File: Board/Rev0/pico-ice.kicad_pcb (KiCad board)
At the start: 2 copper layers, 52 x 51 mm, 34 parts, among them J1 USB_B_Micro, J2 Conn_01x02, J3 Conn_02x18_Odd_Even, J4 Conn_02x18_Odd_Even, U1 NCP1117-3.3_SOT223, U2 W25Q128JVS, U3 RP2040, Y1 ABLS-12.000MHZ-B4-T

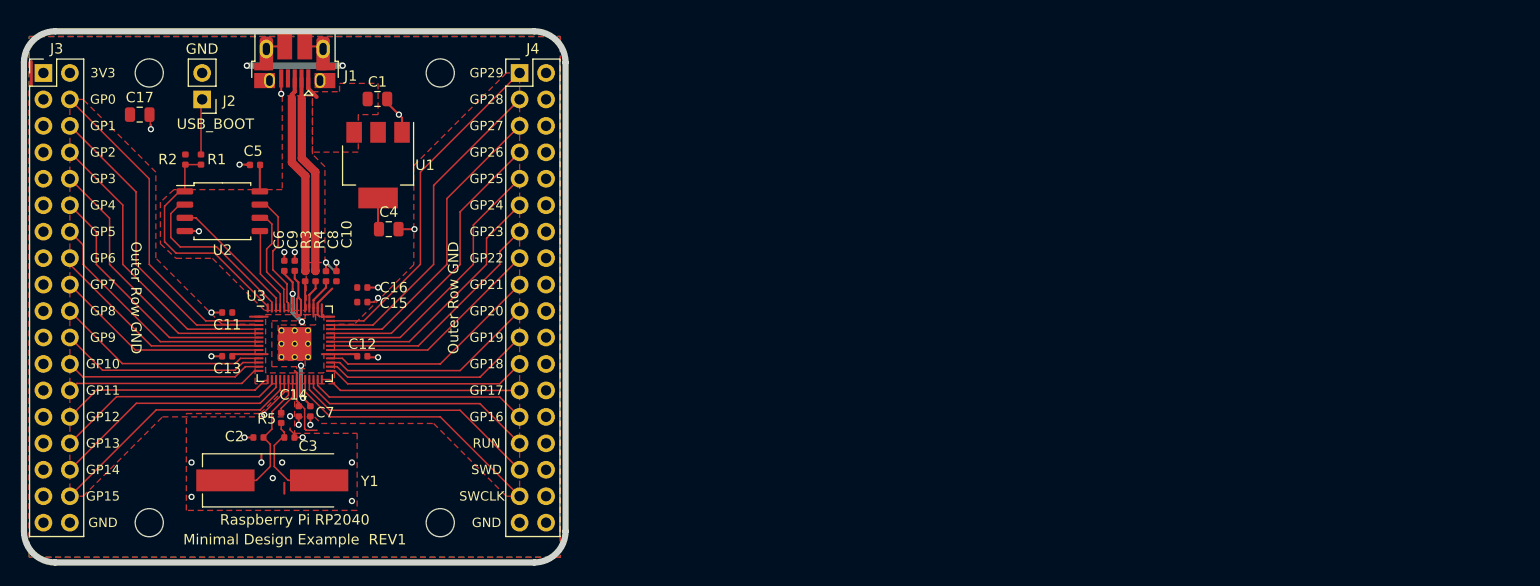
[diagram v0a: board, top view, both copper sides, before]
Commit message: Added MPN and footprint.
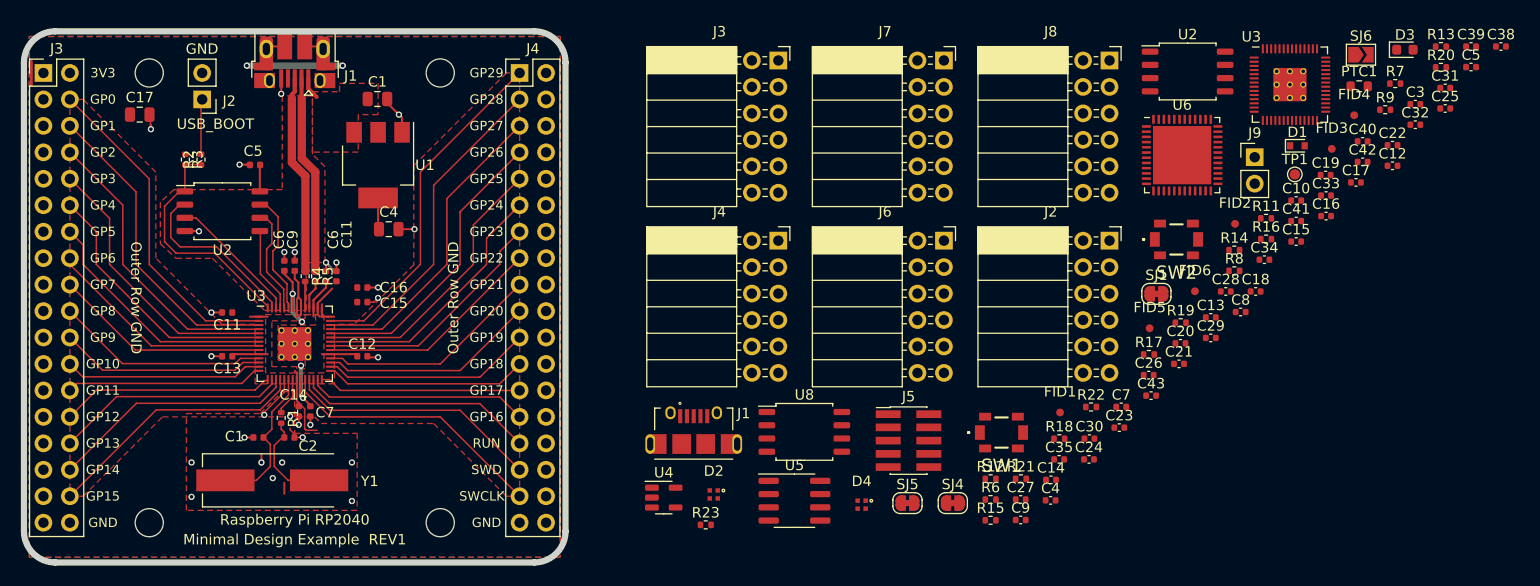
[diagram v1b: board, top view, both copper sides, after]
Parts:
- added C10: 0.1u, Capacitor_SMD:C_0402_1005Metric, F.Cu at (196.2, 86.2)
- added C12: 0.1u, Capacitor_SMD:C_0402_1005Metric, F.Cu at (205.4, 82.9)
- added C13: 4.7u, Capacitor_SMD:C_0402_1005Metric, F.Cu at (187.9, 97.5)
- added C14: 0.1u, Capacitor_SMD:C_0402_1005Metric, F.Cu at (172.6, 113.1)
- added C15: 0.1u, Capacitor_SMD:C_0402_1005Metric, F.Cu at (196.2, 90.2)
- added C16: 0.1u, Capacitor_SMD:C_0402_1005Metric, F.Cu at (199.0, 87.7)
- added C17: 0.1u, Capacitor_SMD:C_0402_1005Metric, F.Cu at (201.9, 84.5)
- added C18: 0.1u, Capacitor_SMD:C_0402_1005Metric, F.Cu at (192.3, 95.0)
- added C19: 0.1u, Capacitor_SMD:C_0402_1005Metric, F.Cu at (199.0, 83.8)
- added C20: 0.1u, Capacitor_SMD:C_0402_1005Metric, F.Cu at (185.0, 100.0)
- added C21: 0.1u, Capacitor_SMD:C_0402_1005Metric, F.Cu at (184.9, 101.9)
- added C22: 4.7u, Capacitor_SMD:C_0402_1005Metric, F.Cu at (205.4, 80.9)
- added C23: 0.1u, Capacitor_SMD:C_0402_1005Metric, F.Cu at (179.2, 108.0)
- added C24: 0.1u, Capacitor_SMD:C_0402_1005Metric, F.Cu at (176.3, 111.1)
- added C25: 4.7u, Capacitor_SMD:C_0402_1005Metric, F.Cu at (210.5, 77.4)
- added C26: 0.1u, Capacitor_SMD:C_0402_1005Metric, F.Cu at (182.0, 103.0)
- added C27: 0.1u, Capacitor_SMD:C_0402_1005Metric, F.Cu at (169.7, 115.0)
- added C28: 0.1u, Capacitor_SMD:C_0402_1005Metric, F.Cu at (189.4, 95.0)
- added C29: 0.1u, Capacitor_SMD:C_0402_1005Metric, F.Cu at (187.9, 99.4)
- added C3: 4.7u, Capacitor_SMD:C_0402_1005Metric, F.Cu at (207.6, 77.0)
- added C30: 4.7u, Capacitor_SMD:C_0402_1005Metric, F.Cu at (176.3, 109.1)
- added C31: 4.7u, Capacitor_SMD:C_0402_1005Metric, F.Cu at (210.5, 75.4)
- added C32: 4.7u, Capacitor_SMD:C_0402_1005Metric, F.Cu at (207.6, 79.0)
- added C33: 0.1u, Capacitor_SMD:C_0402_1005Metric, F.Cu at (199.0, 85.8)
- added C34: 4.7u, Capacitor_SMD:C_0402_1005Metric, F.Cu at (193.1, 91.9)
- added C35: 0.1u, Capacitor_SMD:C_0402_1005Metric, F.Cu at (173.4, 111.1)
- added C38: 0.1u, Capacitor_SMD:C_0402_1005Metric, F.Cu at (215.8, 71.5)
- added C39: 0.1u, Capacitor_SMD:C_0402_1005Metric, F.Cu at (212.9, 71.5)
- added C4: 0.1u, Capacitor_SMD:C_0402_1005Metric, F.Cu at (172.6, 115.0)
- added C40: 0.1u, Capacitor_SMD:C_0402_1005Metric, F.Cu at (202.5, 80.6)
- added C41: 0.1u, Capacitor_SMD:C_0402_1005Metric, F.Cu at (196.2, 88.2)
- added C42: 0.1u, Capacitor_SMD:C_0402_1005Metric, F.Cu at (202.5, 82.5)
- added C43: 4.7u, Capacitor_SMD:C_0402_1005Metric, F.Cu at (182.2, 105.0)
- added C5: 0.1u, Capacitor_SMD:C_0402_1005Metric, F.Cu at (212.9, 73.4)
- added C7: 4.7u, Capacitor_SMD:C_0402_1005Metric, F.Cu at (179.3, 106.1)
- added C8: 0.1u, Capacitor_SMD:C_0402_1005Metric, F.Cu at (190.8, 97.0)
- added C9: 4.7u, Capacitor_SMD:C_0402_1005Metric, F.Cu at (169.7, 116.9)
- added D1: 1N4148WT-7, Diode_SMD:D_SOD-523, F.Cu at (196.3, 81.0)
- added D2: MHPA1010RGBDT, CUSTOM:LED_Cree-PLCC4_1x1mm_CW, F.Cu at (140.2, 114.5)
- added D3: LTST-C191KGKT, LED_SMD:LED_0603_1608Metric, F.Cu at (206.6, 71.8)
- added D4: MHPA1010RGBDT, CUSTOM:LED_Cree-PLCC4_1x1mm_CW, F.Cu at (154.4, 115.5)
- added FID1: Fiducial, Fiducial:Fiducial_0.75mm_Mask1.5mm, F.Cu at (173.5, 106.6)
- added FID2: Fiducial, Fiducial:Fiducial_0.75mm_Mask1.5mm, F.Cu at (190.3, 88.5)
- added FID3: Fiducial, Fiducial:Fiducial_0.75mm_Mask1.5mm, F.Cu at (199.6, 81.3)
- added FID4: Fiducial, Fiducial:Fiducial_0.75mm_Mask1.5mm, F.Cu at (201.7, 78.1)
- added FID5: Fiducial, Fiducial:Fiducial_0.75mm_Mask1.5mm, F.Cu at (182.1, 98.5)
- added FID6: Fiducial, Fiducial:Fiducial_0.75mm_Mask1.5mm, F.Cu at (186.4, 95.0)
- added J1: Connector_USB_B_Micro, CUSTOM:MOLEX_47589-0001, F.Cu at (138.3, 108.9)
- added J2: 6X2 Female Header, CUSTOM:PMOD_2x06_P2.54mm_Horizontal, F.Cu at (178.2, 90.1)
- added J3: 6X2 Female Header, CUSTOM:PMOD_2x06_P2.54mm_Horizontal, F.Cu at (146.4, 72.8)
- added J4: 6X2 Female Header, CUSTOM:PMOD_2x06_P2.54mm_Horizontal, F.Cu at (146.4, 90.1)
- added J5: Conn_ARM_JTAG_SWD_10, Connector_PinHeader_1.27mm:PinHeader_2x05_P1.27mm_Vertical_SMD, F.Cu at (158.9, 109.3)
- added J6: 6X2 Female Header, CUSTOM:PMOD_2x06_P2.54mm_Horizontal, F.Cu at (162.3, 90.1)
- added J7: 6X2 Female Header, CUSTOM:PMOD_2x06_P2.54mm_Horizontal, F.Cu at (162.3, 72.8)
- added J8: 6X2 Female Header, CUSTOM:PMOD_2x06_P2.54mm_Horizontal, F.Cu at (178.2, 72.8)
- added J9: BOOT_SEL, Connector_PinHeader_2.54mm:PinHeader_1x02_P2.54mm_Vertical, F.Cu at (192.2, 82.1)
- added PTC1: MF-FSMF035X-2, Resistor_SMD:R_0603_1608Metric, F.Cu at (202.2, 75.3)
- added R11: 100, Resistor_SMD:R_0402_1005Metric, F.Cu at (193.3, 88.0)
- added R12: 10K, Resistor_SMD:R_0402_1005Metric, F.Cu at (166.8, 113.0)
- added R13: 10K, Resistor_SMD:R_0402_1005Metric, F.Cu at (210.1, 71.5)
- added R14: 2.2K, Resistor_SMD:R_0402_1005Metric, F.Cu at (190.2, 91.0)
- added R15: 10K, Resistor_SMD:R_0402_1005Metric, F.Cu at (166.8, 117.0)
- added R16: 10K, Resistor_SMD:R_0402_1005Metric, F.Cu at (193.3, 90.0)
- added R17: 10K, Resistor_SMD:R_0402_1005Metric, F.Cu at (182.0, 101.0)
- added R18: 2.2K, Resistor_SMD:R_0402_1005Metric, F.Cu at (173.4, 109.1)
- added R19: 2.2K, Resistor_SMD:R_0402_1005Metric, F.Cu at (185.1, 98.0)
- added R20: 2.2K, Resistor_SMD:R_0402_1005Metric, F.Cu at (210.1, 73.5)
- added R21: 10K, Resistor_SMD:R_0402_1005Metric, F.Cu at (169.7, 113.0)
- added R22: 27, Resistor_SMD:R_0402_1005Metric, F.Cu at (176.5, 106.1)
- added R23: 27, Resistor_SMD:R_0402_1005Metric, F.Cu at (139.5, 117.4)
- added R6: 27, Resistor_SMD:R_0402_1005Metric, F.Cu at (166.8, 115.0)
- added R7: 10K, Resistor_SMD:R_0402_1005Metric, F.Cu at (205.7, 75.0)
- added R8: 10K, Resistor_SMD:R_0402_1005Metric, F.Cu at (190.2, 93.0)
- added R9: 10K, Resistor_SMD:R_0402_1005Metric, F.Cu at (204.7, 77.5)
- added SJ1: SHORT, Jumper:SolderJumper-2_P1.3mm_Bridged_RoundedPad1.0x1.5mm, F.Cu at (182.7, 95.2)
- added SJ4: SHORT, Jumper:SolderJumper-2_P1.3mm_Bridged_RoundedPad1.0x1.5mm, F.Cu at (163.2, 115.3)
- added SJ5: SHORT, Jumper:SolderJumper-2_P1.3mm_Bridged_RoundedPad1.0x1.5mm, F.Cu at (158.8, 115.3)
- added SJ6: OPEN, Jumper:SolderJumper-2_P1.3mm_Open_TrianglePad1.0x1.5mm, F.Cu at (202.4, 72.2)
- added SW1: PTS820 J25K SMTR LFS, CUSTOM:PTS820J25KSMTRLFS, F.Cu at (167.9, 108.5)
- added SW2: PTS820 J25K SMTR LFS, CUSTOM:PTS820J25KSMTRLFS, F.Cu at (184.7, 90.0)
- added TP1: TestPoint, TestPoint:TestPoint_Pad_D1.0mm, F.Cu at (196.0, 83.7)
- added U2: W25Q32JVSSIQ, Package_SO:SOIC-8_5.23x5.23mm_P1.27mm, F.Cu at (185.7, 73.9)
- added U3: RP2040, RP2040_minimal:RP2040-QFN-56, F.Cu at (195.6, 75.1)
- added U4: CL9293A12L5M, Package_TO_SOT_SMD:SOT-23-5, F.Cu at (135.4, 114.8)
- added U5: APS6404L-3SQN-SN, Package_SO:SOIC-8_3.9x4.9mm_P1.27mm, F.Cu at (148.0, 115.1)
- added U6: ICE40UP5K-SG48ITR, Package_DFN_QFN:QFN-48-1EP_7x7mm_P0.5mm_EP5.6x5.6mm, F.Cu at (185.2, 81.9)
- added U8: W25Q32JVSSIQ, Package_SO:SOIC-8_5.23x5.23mm_P1.27mm, F.Cu at (148.9, 108.5)
- R1: renamed from R5; footprint Capacitor_SMD:C_0402_1005Metric -> Resistor_SMD:R_0402_1005Metric
- R2: renamed from R1; footprint Capacitor_SMD:C_0402_1005Metric -> Resistor_SMD:R_0402_1005Metric
- R3: renamed from R2; value DNF -> DNP; footprint Capacitor_SMD:C_0402_1005Metric -> Resistor_SMD:R_0402_1005Metric
- R4: renamed from R3; footprint Capacitor_SMD:C_0402_1005Metric -> Resistor_SMD:R_0402_1005Metric
- R5: renamed from R4; footprint Capacitor_SMD:C_0402_1005Metric -> Resistor_SMD:R_0402_1005Metric
- U1: value NCP1117-3.3_SOT223 -> NCP1117ST33T3G
- renumbered C2 to C1, C10 to C11, C3 to C2, C8 to C6
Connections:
- net /~USB_BOOT renamed /~{USB_BOOT}
- R4 pad 2: Net-(R3-Pad2) -> Net-(R4-Pad2)
- R5 pad 2: Net-(R4-Pad2) -> Net-(R5-Pad2)
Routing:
- net Net-(R5-Pad2): track 0.00 -> 2.81 mm
- net Net-(R3-Pad2): track 2.56 -> 0.00 mm
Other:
- net class Default removed
- net class USB_DIFF_90 removed
